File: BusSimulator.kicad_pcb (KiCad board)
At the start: 2 copper layers, 101.6 x 53.4 mm, 100 parts, among them IC1 CS30CL, IC2 CS30CL, IC3 CS30CL, J1 CONN_3-6318491-6, J2 OSTTA024163, J3 Conn_01x03, J4 Conn_01x03, J5 Conn_01x02, J6 Conn_01x03, Q1 MOSFET_N, Q2 MOSFET_N, Q3 MOSFET_N, U1 MPM3620, U2 MPM3620, U3 MCP6H04-E/SL, U4 ADC128D818CIMTX, U5 ISO1540DR, U6 ISOInputs_Si8660_SOIC-16, U7 ISOOutputs_Si8660_SOIC-16, U8 ISOOutputs_Si8660_SOIC-16, U9 MSATA-Socket

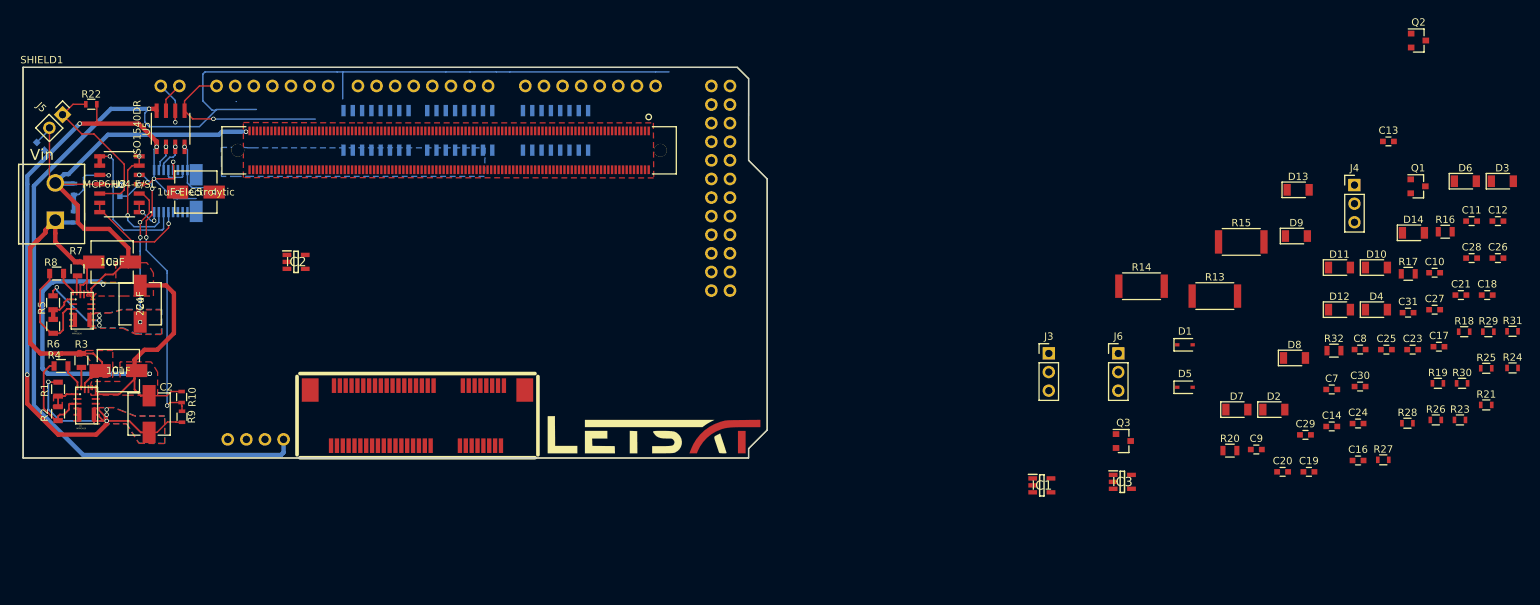
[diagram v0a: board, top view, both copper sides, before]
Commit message: Routed mCOM connector and isolators
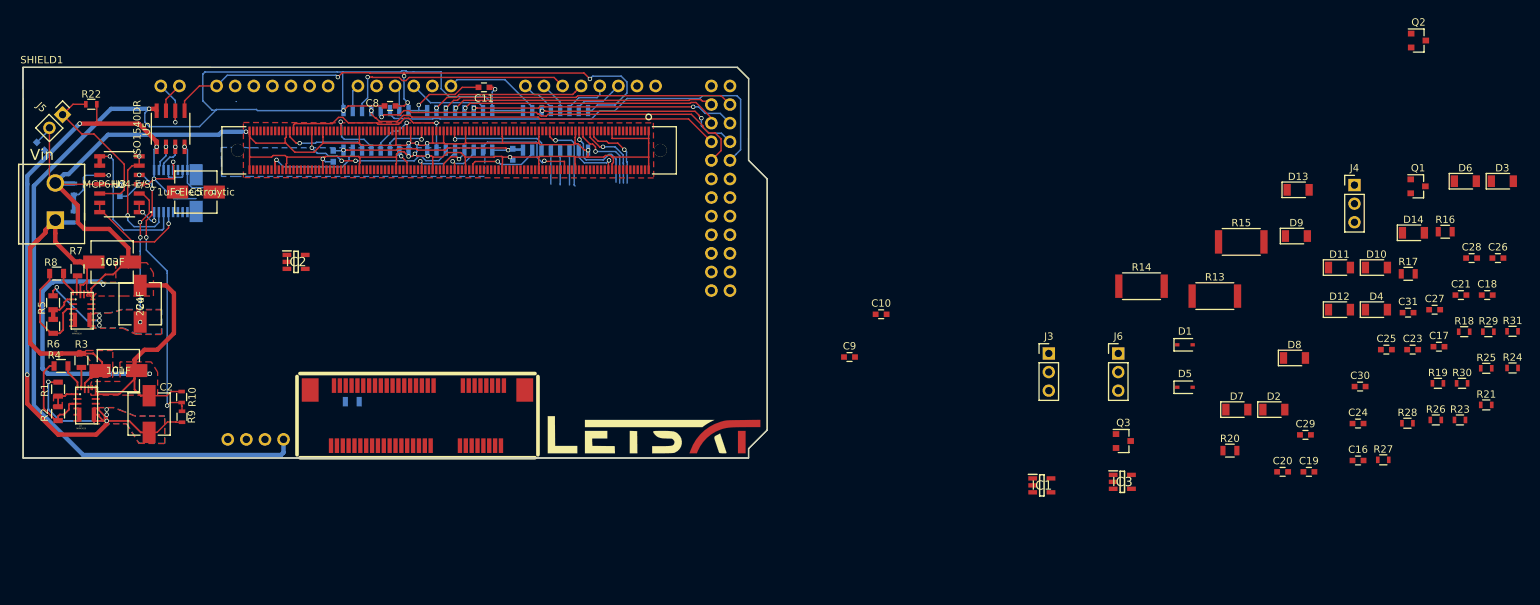
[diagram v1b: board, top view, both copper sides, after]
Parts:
- removed C13, C14: .1uF, Capacitors_SMD:C_0603
- C12, C7, R32: moved to B.Cu
- moved C12 159.3 mm to (152.5, 100.7), turned to 270 degrees
- moved C8 136.6 mm to (160.3, 93.9)
- moved C11 136.1 mm to (173.1, 91.3), turned to 180 degrees
- moved R32 134.2 mm to (155.1, 134.2)
- moved C7 116.4 mm to (177.0, 100.4), turned to 270 degrees
- moved C10 75.8 mm to (227.3, 122.3)
- moved C9 57.0 mm to (223.0, 128.1)
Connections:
- SHIELD1 pad 22: ISO_GPI3 -> ISO_GPO3
- SHIELD1 pad 23: ISO_GPI2 -> ISO_GPO0
- SHIELD1 pad 24: ISO_GPI1 -> ISO_GPO2
- SHIELD1 pad 25: ISO_GPI0 -> ISO_GPO1
- SHIELD1 pad 26: ISO_GPO3 -> ISO_GPI3
- SHIELD1 pad 27: ISO_GPO2 -> ISO_GPI0
- SHIELD1 pad 28: ISO_GPO1 -> ISO_GPI2
- SHIELD1 pad 29: ISO_GPO0 -> ISO_GPI1
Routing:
- net mCOM_GND: track 129.0 -> 298.2 mm, vias 4 -> 13
- net GND: track 25.6 -> 92.7 mm, vias 1 -> 5
- net ISO_GPI1: track 0.00 -> 59.1 mm
- net ISO_GPI2: track 0.00 -> 53.0 mm, vias 0 -> 1
- net ISO_GPI3: track 0.00 -> 49.2 mm, vias 0 -> 1
- net ISO_GPO0: track 0.00 -> 40.0 mm, vias 0 -> 1
- net ISO_GPO1: track 0.00 -> 36.0 mm, vias 0 -> 2
- net ISO_GPO3: track 0.00 -> 35.6 mm, vias 0 -> 1
- net ISO_GPO2: track 0.00 -> 35.5 mm, vias 0 -> 1
- net ISOSERO_Tx: track 0.00 -> 32.4 mm, vias 0 -> 1
- net +3.3V: track 29.7 -> 60.9 mm, vias 7 -> 9
- net ISO_GPI0: track 0.00 -> 28.0 mm, vias 0 -> 2
- net mCOM_TX: track 0.00 -> 25.5 mm, vias 0 -> 1
- net GPO0: track 0.00 -> 22.7 mm, vias 0 -> 3
- net ISOSERO_Rx: track 0.00 -> 21.0 mm, vias 0 -> 1
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
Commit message: added leds
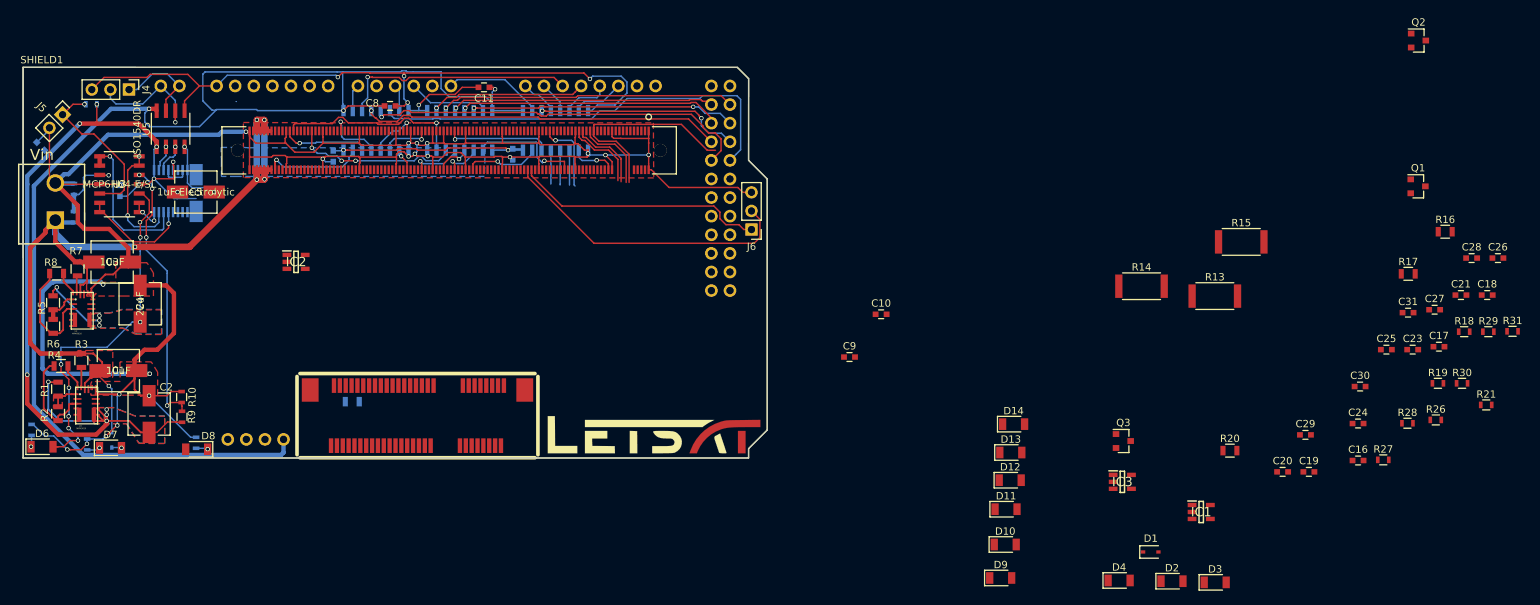
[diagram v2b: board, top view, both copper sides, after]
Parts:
- removed J3: Conn_01x03, Pin_Headers:Pin_Header_Straight_1x03_Pitch2.54mm
- D5, R22, R23, R24, R25: moved to B.Cu
- moved D6 197.7 mm to (112.8, 140.4)
- moved R23 195.1 mm to (111.3, 138.1), turned to 270 degrees
- moved R24 194.9 mm to (118.9, 140.1), turned to 270 degrees
- moved R25 176.5 mm to (133.8, 139.8), turned to 270 degrees
- moved J4 167.8 mm to (124.6, 91.6), turned to 270 degrees
- moved D7 153.9 mm to (122.1, 140.5)
- moved D8 150.4 mm to (133.9, 140.7), turned to 180 degrees
- moved D5 146.7 mm to (122.3, 139.4), turned to 270 degrees
- moved D3 67.4 mm to (273.0, 158.9)
- moved D10 63.2 mm to (244.3, 153.7)
- moved D9 61.7 mm to (243.7, 158.3)
- moved D14 60.5 mm to (245.4, 137.3)
- moved D11 56.2 mm to (244.4, 148.9)
- moved D13 53.2 mm to (245.1, 141.2)
- moved J6 52.9 mm to (209.6, 110.7), turned to 180 degrees
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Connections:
- C25 pad 1: (no net) -> FC5V
- C29 pad 1: (no net) -> Net-(C29-Pad1)
- C30 pad 1: (no net) -> Net-(C30-Pad1)
- C31 pad 1: (no net) -> Net-(C31-Pad1)
- D5 pad 1: mCOM_12V -> 12v_sense
- J1 pad 10: (no net) -> Net-(J1-Pad10)
- J1 pad 101: (no net) -> Net-(J1-Pad101)
- J1 pad 102: (no net) -> Net-(J1-Pad102)
- J1 pad 103: (no net) -> Net-(J1-Pad103)
- J1 pad 104: mCOM_12V -> 12v_sense
- J1 pad 105: mCOM_12V -> 12v_sense
- J1 pad 106: mCOM_12V -> 12v_sense
- J1 pad 107: mCOM_12V -> 12v_sense
- J1 pad 108: mCOM_12V -> 12v_sense
- J1 pad 109: mCOM_12V -> 12v_sense
- J1 pad 112: (no net) -> Net-(J1-Pad112)
- J1 pad 113: (no net) -> Net-(J1-Pad113)
- J1 pad 114: (no net) -> Net-(J1-Pad114)
- J1 pad 115: (no net) -> Net-(J1-Pad115)
- J1 pad 12: (no net) -> Net-(J1-Pad12)
- J1 pad 123: (no net) -> Net-(J1-Pad123)
- J1 pad 124: (no net) -> Net-(J1-Pad124)
- J1 pad 125: (no net) -> Net-(J1-Pad125)
- J1 pad 126: (no net) -> Net-(J1-Pad126)
- J1 pad 127: (no net) -> Net-(J1-Pad127)
- J1 pad 128: (no net) -> Net-(J1-Pad128)
- J1 pad 129: (no net) -> Net-(J1-Pad129)
- J1 pad 13: (no net) -> Net-(J1-Pad13)
- J1 pad 130: (no net) -> Net-(J1-Pad130)
- J1 pad 132: (no net) -> Net-(J1-Pad132)
- J1 pad 133: (no net) -> Net-(J1-Pad133)
- J1 pad 135: (no net) -> Net-(J1-Pad135)
- J1 pad 136: (no net) -> Net-(J1-Pad136)
- J1 pad 137: (no net) -> Net-(J1-Pad137)
- J1 pad 138: (no net) -> Net-(J1-Pad138)
- J1 pad 139: (no net) -> Net-(J1-Pad139)
- J1 pad 14: (no net) -> Net-(J1-Pad14)
- J1 pad 140: (no net) -> Net-(J1-Pad140)
- J1 pad 142: (no net) -> Net-(J1-Pad142)
- J1 pad 145: (no net) -> Net-(J1-Pad145)
- J1 pad 146: (no net) -> Net-(J1-Pad146)
- J1 pad 147: (no net) -> Net-(J1-Pad147)
- J1 pad 148: (no net) -> Net-(J1-Pad148)
- J1 pad 149: (no net) -> Net-(J1-Pad149)
- J1 pad 15: (no net) -> Net-(J1-Pad15)
- J1 pad 150: (no net) -> Net-(J1-Pad150)
- J1 pad 152: (no net) -> Net-(J1-Pad152)
- J1 pad 153: (no net) -> Net-(J1-Pad153)
- J1 pad 154: (no net) -> Net-(J1-Pad154)
- J1 pad 155: (no net) -> Net-(J1-Pad155)
- J1 pad 156: (no net) -> Net-(J1-Pad156)
- J1 pad 157: (no net) -> Net-(J1-Pad157)
- J1 pad 158: (no net) -> Net-(J1-Pad158)
- J1 pad 160: (no net) -> Net-(J1-Pad160)
- J1 pad 162: (no net) -> Net-(J1-Pad162)
- J1 pad 163: (no net) -> Net-(J1-Pad163)
- J1 pad 165: (no net) -> Net-(J1-Pad165)
- J1 pad 166: (no net) -> Net-(J1-Pad166)
- J1 pad 168: (no net) -> Net-(J1-Pad168)
- J1 pad 169: (no net) -> Net-(J1-Pad169)
- J1 pad 171: (no net) -> Net-(J1-Pad171)
- J1 pad 172: (no net) -> Net-(J1-Pad172)
- J1 pad 174: (no net) -> Net-(J1-Pad174)
- J1 pad 175: (no net) -> Net-(J1-Pad175)
- J1 pad 176: (no net) -> Net-(J1-Pad176)
- J1 pad 178: (no net) -> Net-(J1-Pad178)
- J1 pad 179: (no net) -> Net-(J1-Pad179)
- J1 pad 18: (no net) -> Net-(J1-Pad18)
- J1 pad 181: (no net) -> Net-(J1-Pad181)
- J1 pad 182: (no net) -> Net-(J1-Pad182)
- J1 pad 183: (no net) -> Net-(J1-Pad183)
- J1 pad 184: (no net) -> Net-(J1-Pad184)
- J1 pad 185: (no net) -> Net-(J1-Pad185)
- J1 pad 186: (no net) -> Net-(J1-Pad186)
- J1 pad 187: (no net) -> Net-(J1-Pad187)
- J1 pad 188: (no net) -> Net-(J1-Pad188)
- J1 pad 189: (no net) -> Net-(J1-Pad189)
- J1 pad 191: (no net) -> Net-(J1-Pad191)
- J1 pad 192: (no net) -> Net-(J1-Pad192)
- J1 pad 193: (no net) -> Net-(J1-Pad193)
- J1 pad 198: (no net) -> Net-(J1-Pad198)
- J1 pad 199: (no net) -> Net-(J1-Pad199)
- J1 pad 2: (no net) -> Net-(J1-Pad2)
- J1 pad 201: (no net) -> Net-(J1-Pad201)
- J1 pad 202: (no net) -> Net-(J1-Pad202)
- J1 pad 203: (no net) -> Net-(J1-Pad203)
- J1 pad 204: (no net) -> Net-(J1-Pad204)
- J1 pad 205: (no net) -> Net-(J1-Pad205)
- J1 pad 206: (no net) -> Net-(J1-Pad206)
- J1 pad 207: (no net) -> Net-(J1-Pad207)
- J1 pad 208: (no net) -> Net-(J1-Pad208)
- J1 pad 209: (no net) -> Net-(J1-Pad209)
- J1 pad 211: (no net) -> Net-(J1-Pad211)
- J1 pad 212: (no net) -> Net-(J1-Pad212)
- J1 pad 214: mCOM_12V -> 12v_sense
- J1 pad 215: mCOM_12V -> 12v_sense
- J1 pad 216: mCOM_12V -> 12v_sense
- J1 pad 217: mCOM_12V -> 12v_sense
- J1 pad 218: mCOM_12V -> 12v_sense
- J1 pad 219: mCOM_12V -> 12v_sense
- J1 pad 22: (no net) -> Net-(J1-Pad22)
- J1 pad 23: (no net) -> Net-(J1-Pad23)
- J1 pad 24: (no net) -> Net-(J1-Pad24)
- J1 pad 25: (no net) -> Net-(J1-Pad25)
- J1 pad 26: (no net) -> Net-(J1-Pad26)
- J1 pad 27: (no net) -> Net-(J1-Pad27)
- J1 pad 29: (no net) -> Net-(J1-Pad29)
- J1 pad 3: (no net) -> Net-(J1-Pad3)
- J1 pad 30: (no net) -> Net-(J1-Pad30)
- J1 pad 32: (no net) -> Net-(J1-Pad32)
- J1 pad 33: (no net) -> Net-(J1-Pad33)
- J1 pad 34: (no net) -> Net-(J1-Pad34)
- J1 pad 35: (no net) -> Net-(J1-Pad35)
- J1 pad 36: (no net) -> Net-(J1-Pad36)
- J1 pad 37: (no net) -> Net-(J1-Pad37)
- J1 pad 38: (no net) -> Net-(J1-Pad38)
- J1 pad 39: (no net) -> Net-(J1-Pad39)
- J1 pad 4: (no net) -> Net-(J1-Pad4)
- J1 pad 40: (no net) -> Net-(J1-Pad40)
- J1 pad 42: (no net) -> Net-(J1-Pad42)
- J1 pad 43: (no net) -> Net-(J1-Pad43)
- J1 pad 44: (no net) -> Net-(J1-Pad44)
- J1 pad 45: (no net) -> Net-(J1-Pad45)
- J1 pad 46: (no net) -> Net-(J1-Pad46)
- J1 pad 47: (no net) -> Net-(J1-Pad47)
- J1 pad 48: (no net) -> Net-(J1-Pad48)
- J1 pad 49: (no net) -> Net-(J1-Pad49)
- J1 pad 5: (no net) -> Net-(J1-Pad5)
- J1 pad 50: (no net) -> Net-(J1-Pad50)
- J1 pad 52: (no net) -> Net-(J1-Pad52)
- J1 pad 53: (no net) -> Net-(J1-Pad53)
- J1 pad 55: (no net) -> Net-(J1-Pad55)
- J1 pad 56: (no net) -> Net-(J1-Pad56)
- J1 pad 58: (no net) -> Net-(J1-Pad58)
- J1 pad 59: (no net) -> Net-(J1-Pad59)
- J1 pad 6: (no net) -> Net-(J1-Pad6)
- J1 pad 61: (no net) -> Net-(J1-Pad61)
- J1 pad 62: (no net) -> Net-(J1-Pad62)
- J1 pad 64: (no net) -> Net-(J1-Pad64)
- J1 pad 65: (no net) -> Net-(J1-Pad65)
- J1 pad 68: (no net) -> Net-(J1-Pad68)
- J1 pad 69: (no net) -> Net-(J1-Pad69)
- J1 pad 7: (no net) -> Net-(J1-Pad7)
- J1 pad 71: (no net) -> Net-(J1-Pad71)
- J1 pad 72: (no net) -> Net-(J1-Pad72)
- J1 pad 73: (no net) -> Net-(J1-Pad73)
- J1 pad 74: (no net) -> Net-(J1-Pad74)
- J1 pad 75: (no net) -> Net-(J1-Pad75)
- J1 pad 76: (no net) -> Net-(J1-Pad76)
- J1 pad 77: (no net) -> Net-(J1-Pad77)
- J1 pad 78: (no net) -> Net-(J1-Pad78)
- J1 pad 79: (no net) -> Net-(J1-Pad79)
- J1 pad 8: (no net) -> Net-(J1-Pad8)
- J1 pad 81: (no net) -> Net-(J1-Pad81)
- J1 pad 82: (no net) -> Net-(J1-Pad82)
- J1 pad 83: (no net) -> Net-(J1-Pad83)
- J1 pad 84: (no net) -> Net-(J1-Pad84)
- J1 pad 86: (no net) -> Net-(J1-Pad86)
- J1 pad 87: (no net) -> Net-(J1-Pad87)
- J1 pad 88: (no net) -> Net-(J1-Pad88)
- J1 pad 89: (no net) -> Net-(J1-Pad89)
- J1 pad 9: (no net) -> Net-(J1-Pad9)
- J1 pad 91: (no net) -> Net-(J1-Pad91)
- J1 pad 92: (no net) -> Net-(J1-Pad92)
- J1 pad 94: (no net) -> Net-(J1-Pad94)
- J1 pad 95: (no net) -> Net-(J1-Pad95)
- J1 pad 96: (no net) -> Net-(J1-Pad96)
- J1 pad 97: (no net) -> Net-(J1-Pad97)
- J4 pad 3: mCOM_GND -> GND
- SHIELD1 pad 10: (no net) -> Net-(SHIELD1-Pad10)
- SHIELD1 pad 11: (no net) -> Net-(SHIELD1-Pad11)
- SHIELD1 pad 12: (no net) -> Net-(SHIELD1-Pad12)
- SHIELD1 pad 13: (no net) -> Net-(SHIELD1-Pad13)
- SHIELD1 pad 20: (no net) -> Net-(SHIELD1-Pad20)
- SHIELD1 pad 21: (no net) -> Net-(SHIELD1-Pad21)
- SHIELD1 pad 3: (no net) -> Net-(SHIELD1-Pad3)
- SHIELD1 pad 30: (no net) -> Net-(SHIELD1-Pad30)
- SHIELD1 pad 31: (no net) -> Net-(SHIELD1-Pad31)
- SHIELD1 pad 38: (no net) -> Net-(SHIELD1-Pad38)
- SHIELD1 pad 39: (no net) -> Net-(SHIELD1-Pad39)
- SHIELD1 pad 40: (no net) -> Net-(SHIELD1-Pad40)
- SHIELD1 pad 41: (no net) -> Net-(SHIELD1-Pad41)
- SHIELD1 pad 42: (no net) -> Net-(SHIELD1-Pad42)
- SHIELD1 pad 43: (no net) -> Net-(SHIELD1-Pad43)
- SHIELD1 pad 6: (no net) -> Net-(SHIELD1-Pad6)
- SHIELD1 pad 8: (no net) -> Net-(SHIELD1-Pad8)
- SHIELD1 pad 9: (no net) -> Net-(SHIELD1-Pad9)
- SHIELD1 pad IO_R: (no net) -> Net-(SHIELD1-PadIO_R)
- SHIELD1 pad RST: (no net) -> Net-(SHIELD1-PadRST)
- U1 pad 11: (no net) -> Net-(U1-Pad11)
- U1 pad 2: (no net) -> Net-(U1-Pad2)
- U1 pad 4: (no net) -> Net-(U1-Pad4)
- U1 pad 5: (no net) -> Net-(U1-Pad5)
- U1 pad 6: (no net) -> Net-(U1-Pad6)
- U2 pad 11: (no net) -> Net-(U2-Pad11)
- U2 pad 2: (no net) -> Net-(U2-Pad2)
- U2 pad 4: (no net) -> Net-(U2-Pad4)
- U2 pad 5: (no net) -> Net-(U2-Pad5)
- U2 pad 6: (no net) -> Net-(U2-Pad6)
- U4 pad 6: (no net) -> Net-(U4-Pad6)
- U4 pad 9: (no net) -> Net-(U4-Pad9)
- U9 pad 1: (no net) -> Net-(U9-Pad1)
- U9 pad 10: (no net) -> Net-(U9-Pad10)
- U9 pad 11: (no net) -> Net-(U9-Pad11)
- U9 pad 12: (no net) -> Net-(U9-Pad12)
- U9 pad 13: (no net) -> Net-(U9-Pad13)
- U9 pad 14: (no net) -> Net-(U9-Pad14)
- U9 pad 16: (no net) -> Net-(U9-Pad16)
- U9 pad 17: (no net) -> Net-(U9-Pad17)
- U9 pad 19: (no net) -> Net-(U9-Pad19)
- U9 pad 20: (no net) -> Net-(U9-Pad20)
- U9 pad 22: (no net) -> Net-(U9-Pad22)
- U9 pad 28: (no net) -> Net-(U9-Pad28)
- U9 pad 3: (no net) -> Net-(U9-Pad3)
- U9 pad 30: (no net) -> Net-(U9-Pad30)
- U9 pad 32: (no net) -> Net-(U9-Pad32)
- U9 pad 36: (no net) -> Net-(U9-Pad36)
- U9 pad 38: (no net) -> Net-(U9-Pad38)
- U9 pad 42: (no net) -> Net-(U9-Pad42)
- U9 pad 43: (no net) -> Net-(U9-Pad43)
- U9 pad 44: (no net) -> Net-(U9-Pad44)
- U9 pad 45: (no net) -> Net-(U9-Pad45)
- U9 pad 46: (no net) -> Net-(U9-Pad46)
- U9 pad 47: (no net) -> Net-(U9-Pad47)
- U9 pad 48: (no net) -> Net-(U9-Pad48)
- U9 pad 5: (no net) -> Net-(U9-Pad5)
- U9 pad 6: (no net) -> Net-(U9-Pad6)
- U9 pad 7: (no net) -> Net-(U9-Pad7)
- U9 pad 8: (no net) -> Net-(U9-Pad8)
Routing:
- net 12v_sense: track 54.9 -> 130.7 mm, vias 0 -> 6
- net mCOM_GND: track 298.2 -> 343.4 mm, vias 13 -> 21
- net I2C_DAT: track 0.00 -> 40.7 mm
- net I2C_CK: track 0.00 -> 34.4 mm
- net +3.3V: track 60.9 -> 91.3 mm, vias 9 -> 14
- net SATA0_TX+: track 10.4 -> 29.4 mm, vias 1 -> 0
- net GND: track 92.7 -> 108.9 mm
- net DUE_SCL: track 7.35 -> 16.8 mm
- net DUE_SDA: track 4.14 -> 12.6 mm
- net SATA0_RX-: track 12.2 -> 10.3 mm, vias 1 -> 0
- net Net-(D7-Pad1): track 0.00 -> 1.81 mm, vias 0 -> 1
- net Net-(D8-Pad1): track 0.00 -> 1.63 mm, vias 0 -> 1
- net Net-(D6-Pad1): track 0.00 -> 1.58 mm, vias 0 -> 1
- net Net-(D5-Pad2): track 0.00 -> 1.34 mm, vias 0 -> 1
- net PWRBTNn: track 6.87 -> 6.23 mm
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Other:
- rule pad_to_mask_clearance: 0.2 -> 0.1

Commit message: zoning fix
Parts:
- moved R32 1.98 mm to (153.2, 134.3)
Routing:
- net mCOM_GND: track 343.4 -> 409.8 mm, vias 21 -> 23
- net SATA_ACTn: track 10.4 -> 75.7 mm, vias 1 -> 2
- net SATA0_TX+: track 29.4 -> 93.5 mm
- net SATA0_TX-: track 10.5 -> 73.3 mm
- net SATA0_RX-: track 10.3 -> 63.3 mm
- net SATA0_RX+: track 11.0 -> 63.9 mm
- net Net-(R32-Pad1): track 0.00 -> 3.05 mm, vias 0 -> 1
- net I2C_DAT: track 40.7 -> 40.9 mm, vias 0 -> 2
- net I2C_CK: track 34.4 -> 34.3 mm, vias 0 -> 2
- added copper zone on F.Cu, net +3.3V
- removed copper zone on F.Cu, net +3V3

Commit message: Fix fill nets
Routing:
- added copper zone on F.Cu, net 12v_sense
- added copper zone on B.Cu, net mCOM_5V_SBY
- added copper zone on F.Cu, net mCOM_5V_SBY
- removed copper zone on B.Cu, net +3V3
- removed copper zone on B.Cu, net +5V
- removed copper zone on F.Cu, net +5V
- removed copper zone on F.Cu, net GNDREF
- removed copper zone on F.Cu, net Net-(C1-Pad2)

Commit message: fix outline
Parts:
- D10, D11, D12, D13, D14, D9: footprint Diodes_SMD:D_1206 -> Diodes_SMD:D_0603
- moved D9 42.7 mm to (210.0, 132.0)
- moved D10 42.4 mm to (210.0, 128.9)
- moved D11 41.3 mm to (210.0, 126.0)
- moved D12 41.3 mm to (210.0, 123.0)
- moved D13 41.0 mm to (210.0, 120.0)
- moved D14 40.8 mm to (210.0, 117.0)
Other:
- board size 101.6 x 53.4 mm -> 109.8 x 53.4 mm

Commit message: Fix edge cut
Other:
- board size 109.8 x 53.4 mm -> 109.9 x 53.3 mm
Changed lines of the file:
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@@
   (general
     (links 470)
-    (no_connects 276)
-    (area 110.084999 88.494999 220.075001 142.025001)
+    (no_connects 273)
+    (area 110.097499 88.507499 220.102501 141.997501)
     (thickness 1.6)
-    (drawings 10)
+    (drawings 19)
     (tracks 1270)
     (zones 0)
@@
     )
   )
-  (gr_line (start 217.46 90.15) (end 215.91 88.6) (layer Edge.Cuts) (width 0.15))
-  (gr_line (start 217.45 101.28) (end 217.46 90.15) (layer Edge.Cuts) (width 0.15))
-  (gr_line (start 220 103.83) (end 217.45 101.28) (layer Edge.Cuts) (width 0.15))
-  (gr_line (start 220 138.11) (end 220 103.83) (layer Edge.Cuts) (width 0.15))
-  (gr_line (start 217.45 140.66) (end 220 138.11) (layer Edge.Cuts) (width 0.15))
-  (gr_line (start 217.45 141.93) (end 217.45 140.66) (layer Edge.Cuts) (width 0.15))
-  (gr_line (start 215.9 88.6) (end 110.16 88.58) (layer Edge.Cuts) (width 0.15))
-  (gr_line (start 110.18 141.93) (end 217.45 141.95) (layer Edge.Cuts) (width 0.15))
-  (gr_line (start 110.16 88.57) (end 110.18 141.93) (layer Edge.Cuts) (width 0.15))
+  (gr_line (start 217.424 90.1065) (end 215.9 88.5825) (layer Edge.Cuts) (width 0.15))
+  (gr_line (start 217.424 90.17) (end 217.424 90.1065) (layer Edge.Cuts) (width 0.15))
+  (gr_line (start 217.424 101.2825) (end 217.424 90.17) (layer Edge.Cuts) (width 0.15))
+  (gr_line (start 220.0275 103.886) (end 217.424 101.2825) (layer Edge.Cuts) (width 0.15))
+  (gr_line (start 220.0275 138.1125) (end 220.0275 103.886) (layer Edge.Cuts) (width 0.15))
+  (gr_line (start 216.2175 141.9225) (end 220.0275 138.1125) (layer Edge.Cuts) (width 0.15))
+  (gr_line (start 110.1725 141.9225) (end 216.2175 141.9225) (layer Edge.Cuts) (width 0.15))
+  (gr_line (start 110.1725 88.5825) (end 110.1725 141.9225) (layer Edge.Cuts) (width 0.15))
+  (gr_line (start 215.9 88.5825) (end 110.1725 88.5825) (layer Edge.Cuts) (width 0.15))
   (gr_text "Vin \n" (at 112.75 100.525) (layer F.SilkS)
     (effects (font (size 1.5 1.5) (thickness 0.3)))

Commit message: finished leds
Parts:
- added D15: LED, Diodes_SMD:D_0603, F.Cu at (211.1, 113.0)
- added D16: LED, Diodes_SMD:D_0603, F.Cu at (211.1, 110.2)
- added R33: 330, Resistors_SMD:R_0603, B.Cu at (208.7, 112.0)
- added R34: 330, Resistors_SMD:R_0603, B.Cu at (210.1, 110.2)
- R30, R31: moved to B.Cu
- moved R31 105.4 mm to (208.7, 114.2), turned to 90 degrees
- moved R29 102.0 mm to (208.3, 121.9), turned to 180 degrees
- moved R30 98.5 mm to (209.0, 118.9), turned to 90 degrees
- moved R26 95.2 mm to (208.3, 127.8), turned to 180 degrees
- moved R28 91.7 mm to (208.3, 125.0), turned to 180 degrees
- moved R27 88.3 mm to (208.3, 130.9), turned to 180 degrees
- moved G1 29.7 mm to (216.5, 117.0), turned to 90 degrees
- moved J6 13.7 mm to (215.2, 98.2)
- moved D10 1.52 mm to (211.1, 127.8)
- moved D11 1.52 mm to (211.1, 124.9)
- moved D12 1.52 mm to (211.1, 121.9)
- moved D13 1.52 mm to (211.1, 118.9)
- moved D14 1.52 mm to (211.1, 115.9)
- moved D9 1.52 mm to (211.1, 130.9)
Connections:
- C23 pad 1: Net-(C23-Pad1) -> 5V_5
- D10 pad 2: FC3V3 -> 5V_5
- D11 pad 2: FC3V3 -> 5V_5
- D12 pad 2: FC3V3 -> 5V_5
- D13 pad 2: FC3V3 -> 5V_5
- D14 pad 2: FC3V3 -> 5V_5
- D9 pad 2: FC3V3 -> 5V_5
- R26 pad 1: Net-(D9-Pad1) -> Net-(D10-Pad1)
- R27 pad 1: Net-(D10-Pad1) -> Net-(D9-Pad1)
- SHIELD1 pad 32: Net-(R31-Pad2) -> Net-(SHIELD1-Pad32)
- SHIELD1 pad 33: Net-(R30-Pad2) -> Net-(SHIELD1-Pad33)
- SHIELD1 pad 34: Net-(R29-Pad2) -> Net-(SHIELD1-Pad34)
- SHIELD1 pad 35: Net-(R28-Pad2) -> Net-(SHIELD1-Pad35)
- SHIELD1 pad 36: Net-(R27-Pad2) -> Net-(R34-Pad2)
- SHIELD1 pad 37: Net-(R26-Pad2) -> Net-(R33-Pad2)
- SHIELD1 pad 38: Net-(SHIELD1-Pad38) -> Net-(R31-Pad2)
- SHIELD1 pad 39: Net-(SHIELD1-Pad39) -> Net-(R30-Pad2)
- SHIELD1 pad 40: Net-(SHIELD1-Pad40) -> Net-(R29-Pad2)
- SHIELD1 pad 41: Net-(SHIELD1-Pad41) -> Net-(R28-Pad2)
- SHIELD1 pad 42: Net-(SHIELD1-Pad42) -> Net-(R27-Pad2)
- SHIELD1 pad 43: Net-(SHIELD1-Pad43) -> Net-(R26-Pad2)
- SHIELD1 pad 5V_5: Net-(C23-Pad1) -> 5V_5
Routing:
- net 5V_5: track 0.00 -> 43.1 mm, vias 0 -> 1
- net mCOM_GND: track 409.8 -> 424.5 mm
- net Net-(R27-Pad2): track 0.00 -> 13.5 mm
- net Net-(R29-Pad2): track 0.00 -> 10.9 mm, vias 0 -> 1
- net I2C_DAT: track 40.9 -> 51.3 mm
- net Net-(R28-Pad2): track 0.00 -> 9.74 mm
- net Net-(R26-Pad2): track 0.00 -> 9.71 mm
- net I2C_CK: track 34.3 -> 42.8 mm, vias 2 -> 3
- net Net-(R34-Pad2): track 0.00 -> 6.78 mm
- net Net-(R31-Pad2): track 0.00 -> 5.61 mm
- net Net-(R30-Pad2): track 0.00 -> 5.12 mm
- net Net-(D16-Pad1): track 0.00 -> 2.83 mm, vias 0 -> 1
- net Net-(D13-Pad1): track 0.00 -> 2.45 mm, vias 0 -> 1
- net Net-(D14-Pad1): track 0.00 -> 2.35 mm, vias 0 -> 1
- net Net-(R33-Pad2): track 0.00 -> 2.00 mm
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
